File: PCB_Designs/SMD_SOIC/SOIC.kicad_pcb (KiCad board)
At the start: 2 copper layers, 40.6 x 17.7 mm, 12 parts, among them J1 USB-AM-S-X-X-TH, U2 ATtiny85-20S, Y1 12MHz

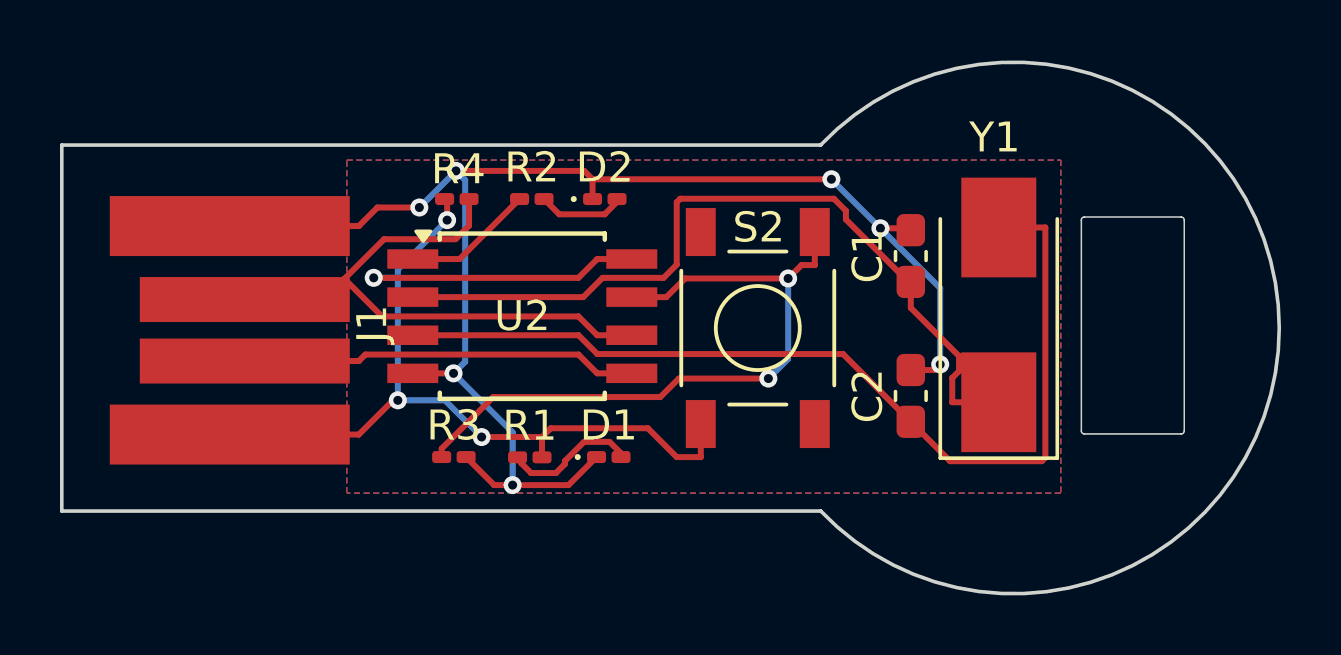
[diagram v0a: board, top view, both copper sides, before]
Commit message: Reposition LEDs on PCB for 3D enclosure alignment
Moved LEDs to new positions on the PCB to ensure proper fit and alignment with the 3D enclosure design. This adjustment accommodates the enclosure's dimensions and improves overall integration.
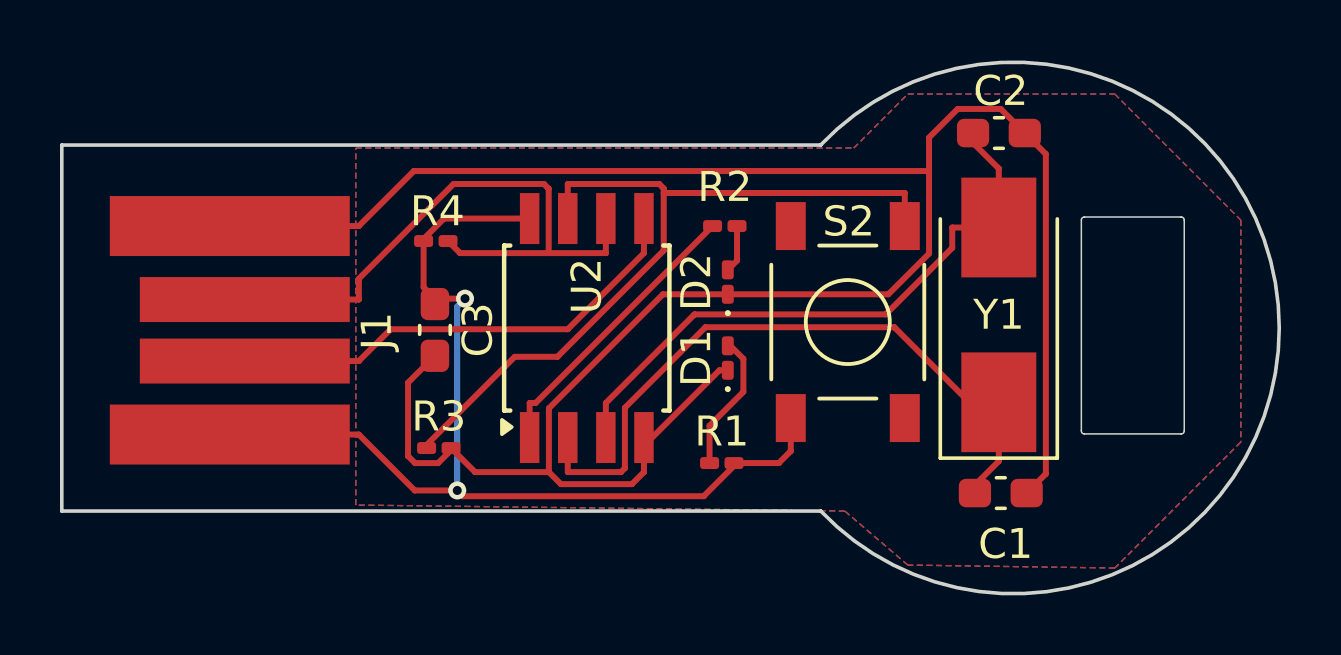
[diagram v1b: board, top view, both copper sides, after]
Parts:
- added C3: 0.1uF, Capacitor_SMD:C_0603_1608Metric_Pad1.08x0.95mm_HandSolder, F.Cu at (150.8, 83.7)
- moved C2 9.24 mm to (169.6, 77.1), turned to 0 degrees
- moved C1 8.45 mm to (169.7, 89.1), turned to 0 degrees
- moved R2 6.50 mm to (160.5, 80.2)
- moved R1 6.40 mm to (160.4, 88.1)
- moved D1 5.16 mm to (160.6, 84.6), turned to 90 degrees
- moved D2 4.95 mm to (160.6, 82.1), turned to 90 degrees
- moved S2 3.01 mm to (164.6, 83.4)
- moved U2 2.19 mm to (155.9, 83.6), turned to 90 degrees
- moved R4 1.57 mm to (150.9, 80.7)
- moved R3 0.59 mm to (151.0, 87.6)
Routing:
- net GND: track 49.4 -> 78.9 mm, vias 7 -> 0
- net Net-(U2-XTAL2/PB4): track 32.1 -> 20.6 mm
- net Net-(U2-~{RESET}/PB5): track 4.39 -> 9.69 mm
- net Net-(U2-XTAL1/PB3): track 26.8 -> 23.5 mm
- net Net-(U2-PB2): track 23.4 -> 26.3 mm, vias 2 -> 0
- net /Data-: track 13.2 -> 15.9 mm
- net Net-(D2-A): track 2.91 -> 1.59 mm
- net /Data+: track 19.7 -> 20.9 mm
- net +5V: track 36.1 -> 35.0 mm, vias 4 -> 2
- added copper zone on B.Cu, net +5V
- added copper zone on F.Cu, net GND
- removed copper zone on F.Cu, net +5V
- removed copper zone on B.Cu, net GND
